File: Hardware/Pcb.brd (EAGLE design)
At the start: 170.2 x 111.2 mm, 103 parts, among them IC1 BD5229G-TR, IC4 XC6220A331MR-G, J1 FH34SRJ-24S-0.5SH_99_, J2 SAMACSYS_PARTS_USB4110-GF-A, J3 QWIIC_RIGHT_ANGLE, J4 112A-TAAR-R03_ATTEND, Q1 20V/4.2A/52mΩ/1.4W, Q2 20V/4.2A/52mΩ/1.4W, Q3 SI1308EDL-T1-GE3, U1 W25Q512JVEIQ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

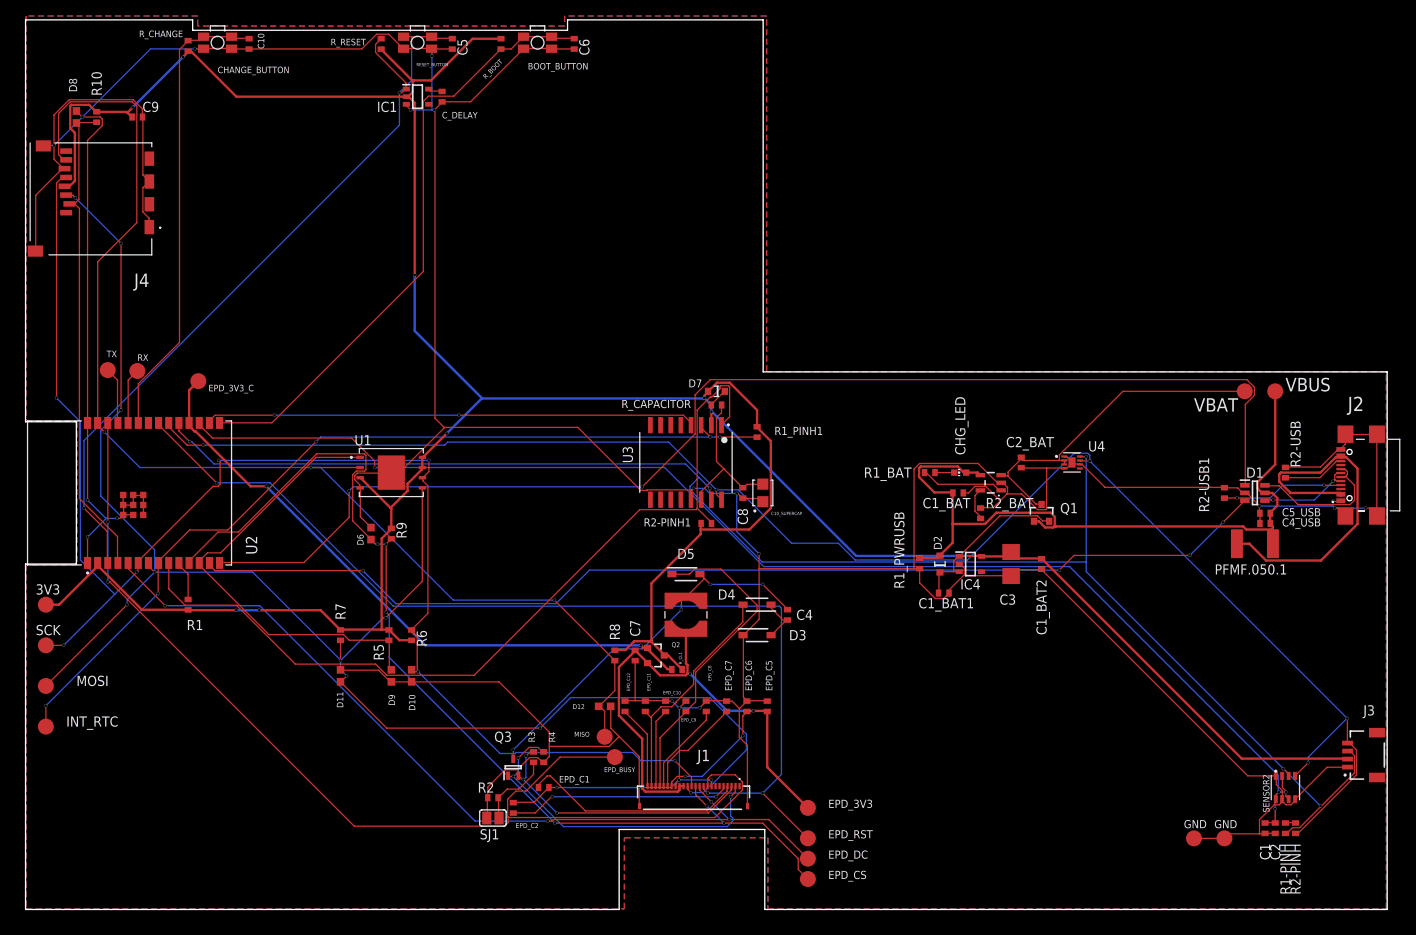
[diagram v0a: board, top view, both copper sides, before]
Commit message: Refăcut via-stitching și planul de masă – close #1, close #3
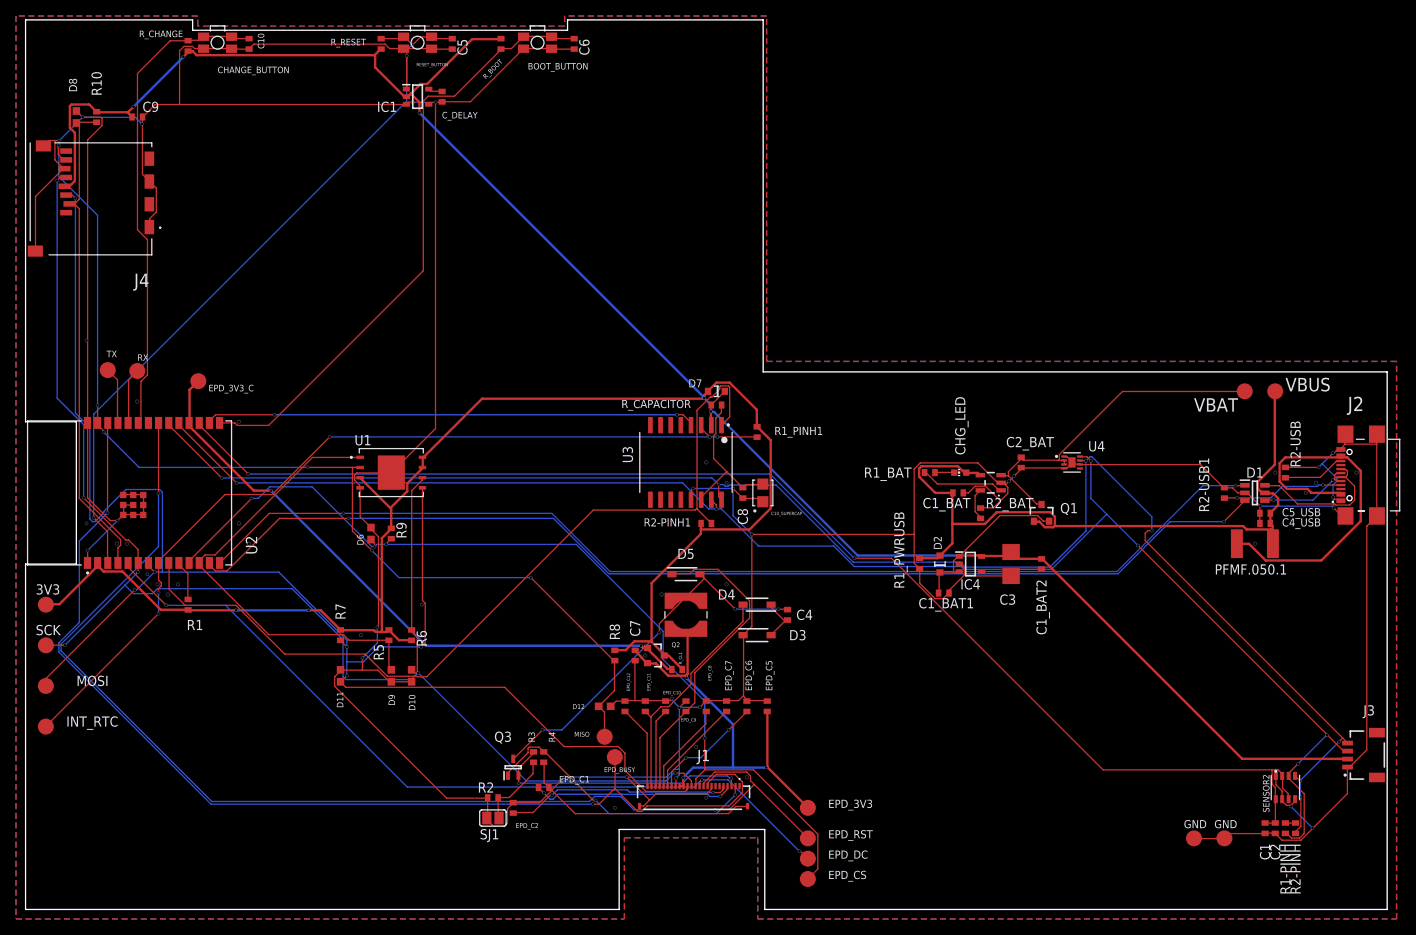
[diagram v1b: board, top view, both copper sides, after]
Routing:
- net EPD_RST: track 127.6 -> 148.0 mm, vias 3 -> 2
- net MISO: track 152.6 -> 132.6 mm, vias 3 -> 6
- net USB_D+: track 156.8 -> 138.2 mm
- net GND: track 730.5 -> 717.9 mm, vias 23 -> 55
- net EPD_3V3: track 64.4 -> 53.9 mm, vias 2 -> 3
- net EPD_CS: track 128.8 -> 118.7 mm, vias 6 -> 4
- net 3V3: track 404.2 -> 411.8 mm, vias 9 -> 8
- net GDR: track 42.3 -> 35.9 mm, vias 3 -> 2
- net EPD_DC: track 106.6 -> 102.3 mm, vias 4 -> 3
- net MOSI: track 204.0 -> 200.1 mm, vias 10 -> 6
- net SCL: track 205.7 -> 202.1 mm, vias 5 -> 7
- net SCK: track 186.0 -> 182.6 mm, vias 7 -> 6
- net RESET: track 99.4 -> 96.2 mm
- net SDA: track 200.0 -> 197.4 mm, vias 5 -> 6
- net N$26: track 27.9 -> 25.4 mm, vias 0 -> 2
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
